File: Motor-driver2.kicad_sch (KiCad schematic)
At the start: 32 parts, among them J12 PINHD_1x4_Male, J15 PINHD_1x4_Male, U4 DRV8825PWP, U5 DRV8825PWP

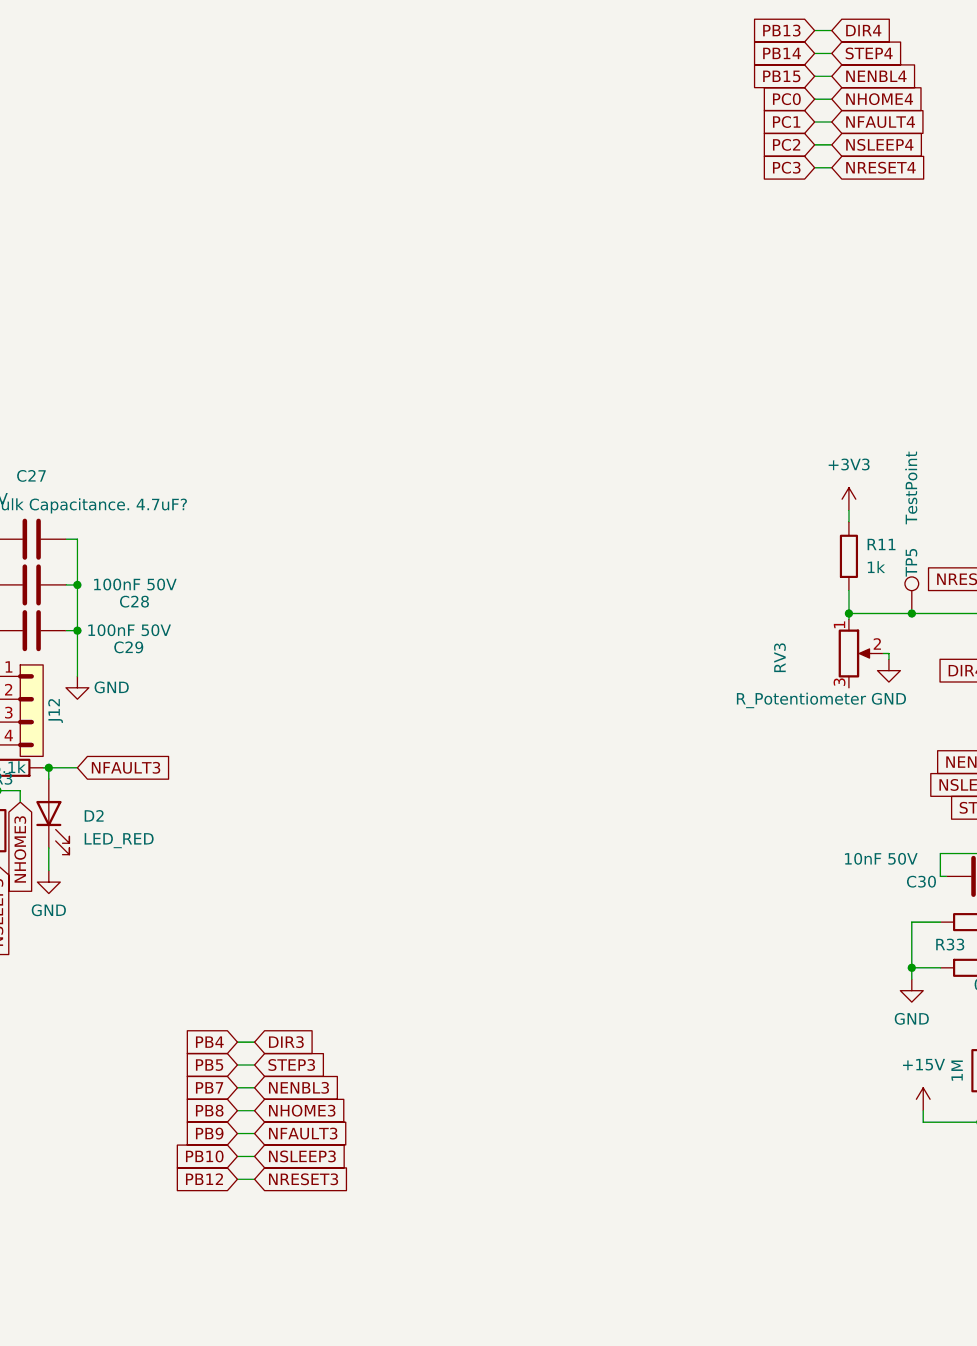
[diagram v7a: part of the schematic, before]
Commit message: finished PCB. DRC 0 errors
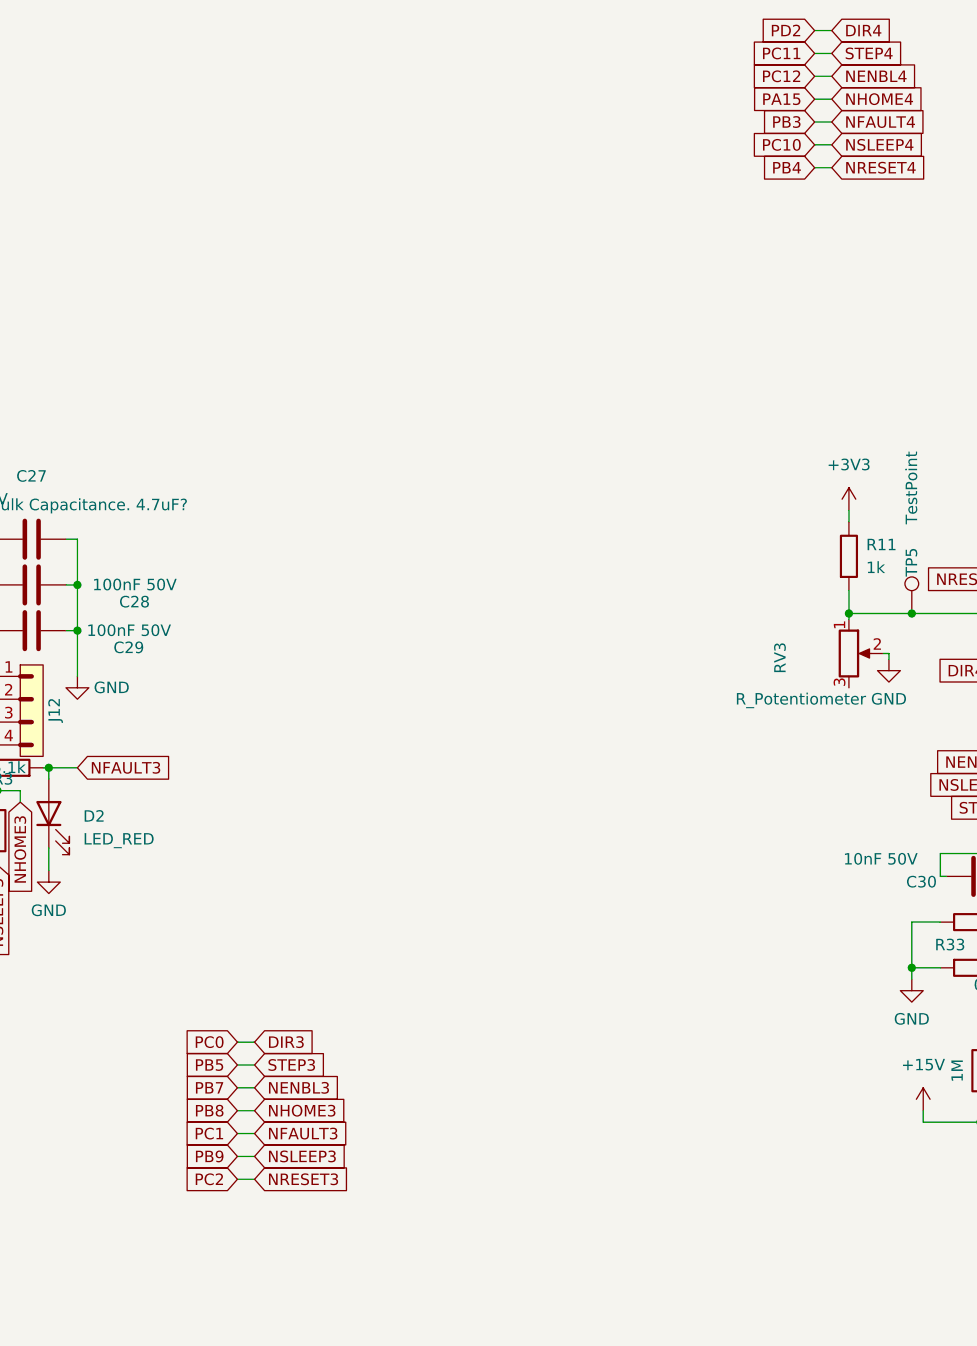
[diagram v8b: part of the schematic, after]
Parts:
- TP2, TP5: footprint TestPoint:TestPoint_Pad_D2.5mm -> TestPoint:TestPoint_Pad_D1.5mm
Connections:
- net PB14 renamed PC11
